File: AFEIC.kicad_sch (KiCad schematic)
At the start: 37 parts, among them J4 CONN HEADER VERT 6POS 1.5MM, U1 TLE9012DQUXUMA1

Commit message: started layout
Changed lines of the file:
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@@
 	(text "For IFH_H/IFH_L's termination resistors:\nIf daisy chain is used, then desolder resistors\nIf daisy chain is not used, solder resistors"
 		(exclude_from_sim no)
-		(at 78.232 118.872 0)
+		(at 70.866 119.126 0)
 		(effects
 			(font

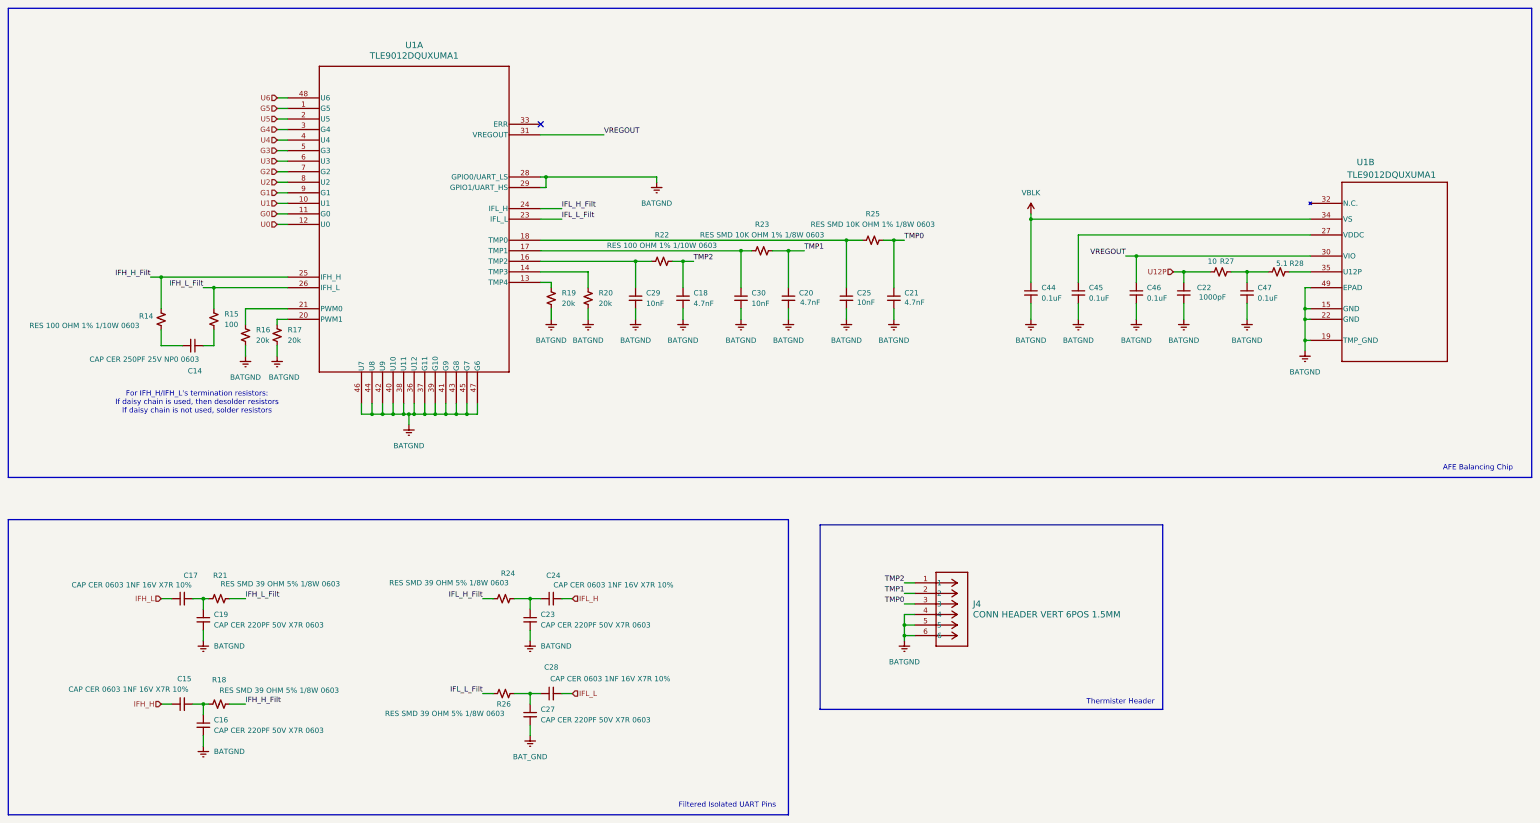
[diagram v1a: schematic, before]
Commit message: initial component layout
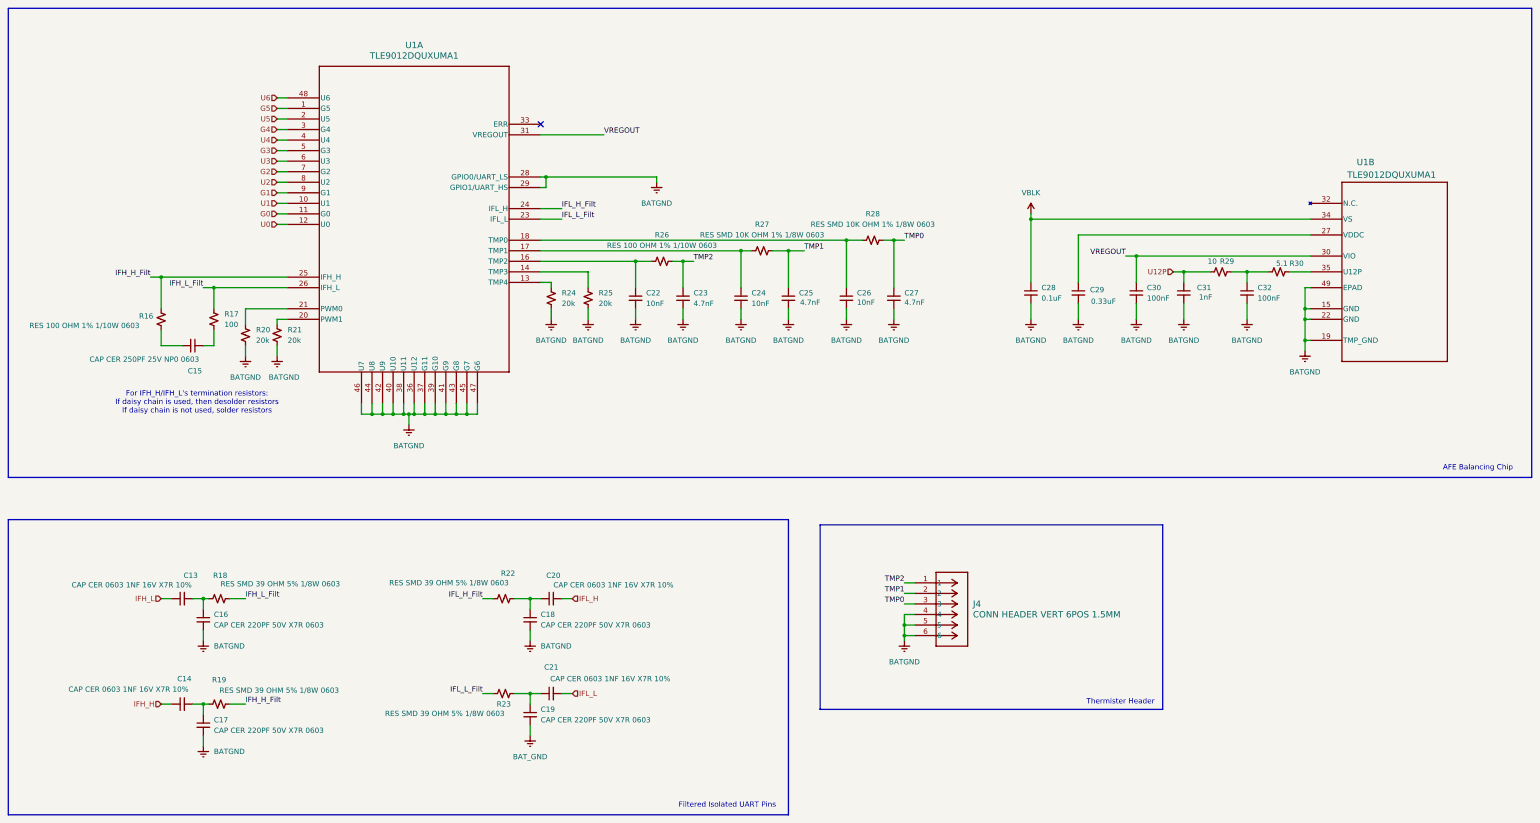
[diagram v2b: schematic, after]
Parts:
- removed C45: 0.1uF, Capacitor_SMD:C_0603_1608Metric, symbol Device:C_Small
- added C29: 0.33uF, Capacitor_SMD:C_0603_1608Metric, symbol Device:C_Small
- C30: renamed from C46; value 0.1uF -> 100nF
- C31: renamed from C22; value 1000pF -> 1nF
- C32: renamed from C47; value 0.1uF -> 100nF
- renumbered C17 to C13, C15 to C14, C14 to C15, C19 to C16, C16 to C17, C23 to C18, C27 to C19, C24 to C20, C28 to C21, C29 to C22, C18 to C23, C30 to C24, C20 to C25, C25 to C26, C21 to C27, C44 to C28, R14 to R16, R15 to R17, R21 to R18, R18 to R19, R16 to R20, R17 to R21, R24 to R22, R26 to R23, R19 to R24, R20 to R25, R22 to R26, R23 to R27, R25 to R28, R27 to R29, R28 to R30
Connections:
- net BATGND: now also C29.2
- net at U1.27 (VDDC): now also C29.1
